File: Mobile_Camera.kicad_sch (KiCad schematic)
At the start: 22 parts, among them J1 SWD_header, J2 DVP_24_pin, J3 Micro_SD_card, SW1 Switch_reset, SW2 Switch_power_on, U1 STM32H753VIT6, Y1 Crystal

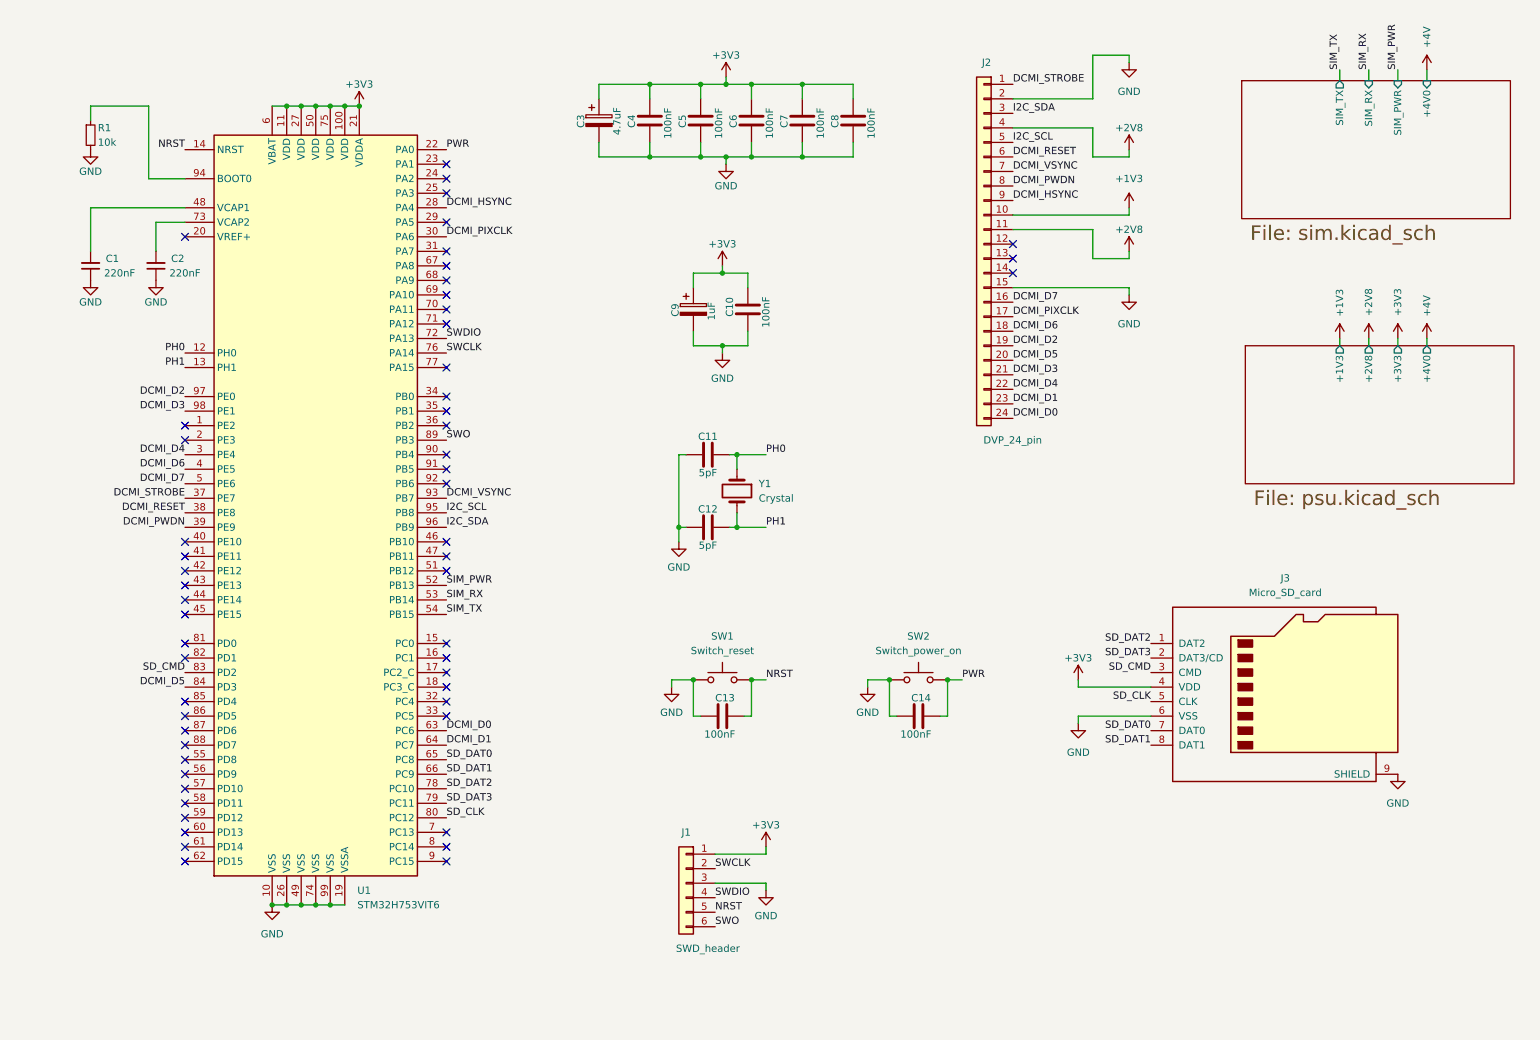
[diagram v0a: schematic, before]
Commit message: Complete the schematic, Begin to layout elements
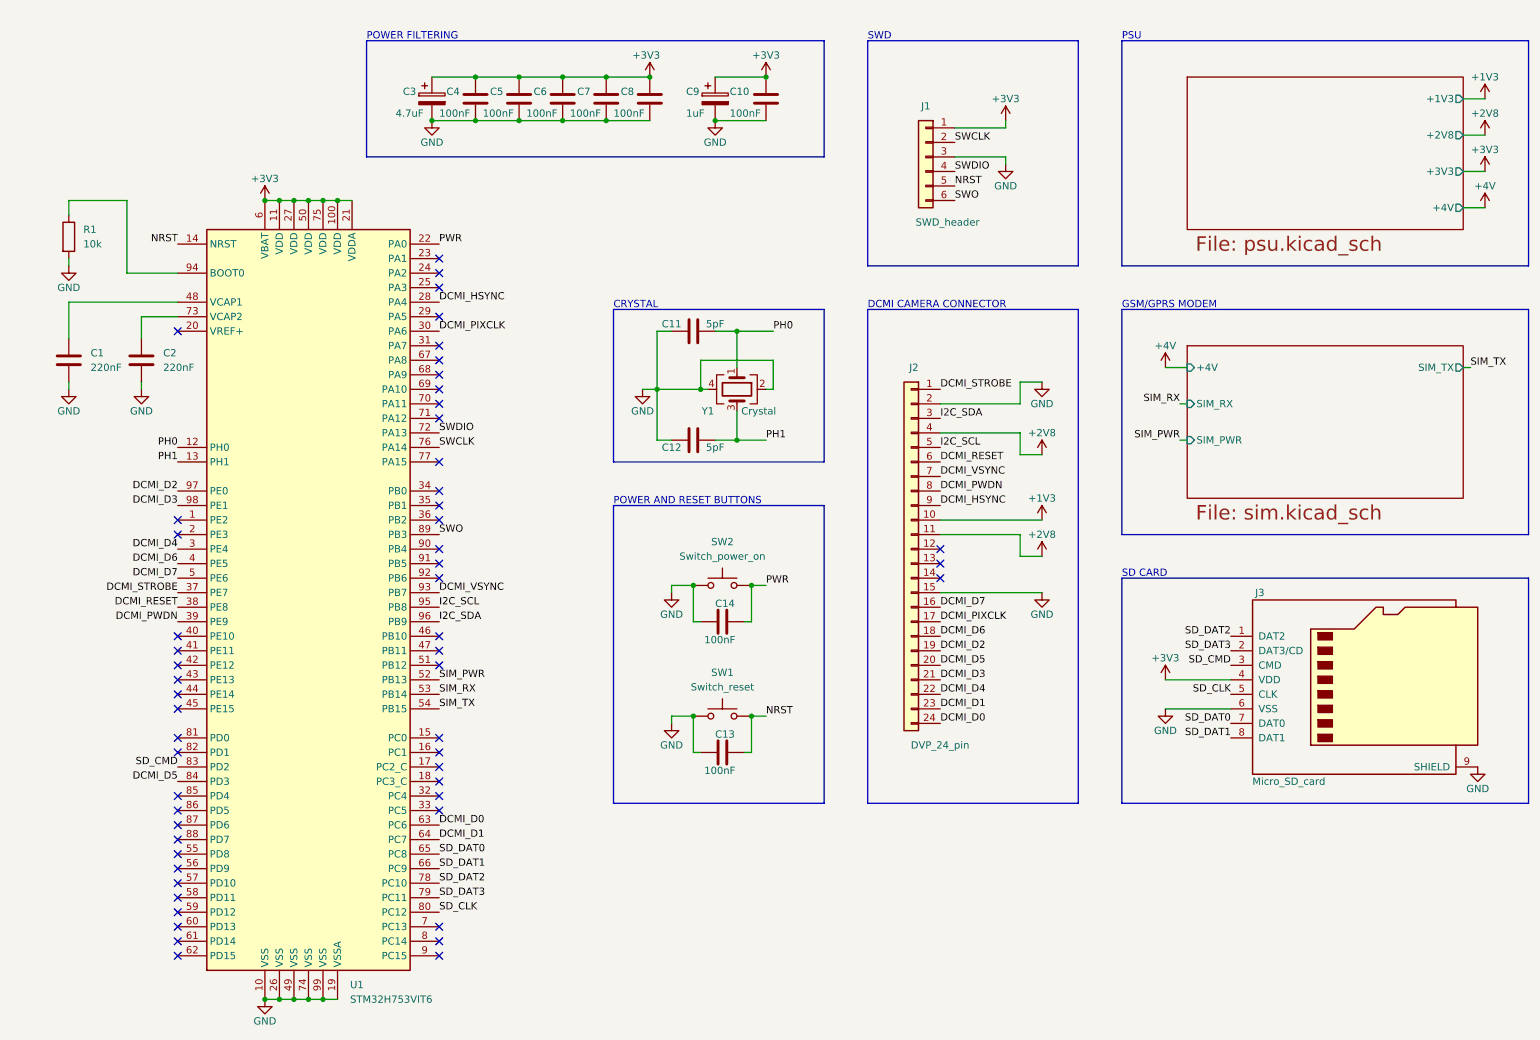
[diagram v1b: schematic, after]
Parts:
- removed C1, C2: 220nF, Capacitor_SMD:C_0603_1608Metric_Pad1.08x0.95mm_HandSolder, symbol Device:C_Small
- removed R1: 10k, Resistor_SMD:R_0603_1608Metric_Pad0.98x0.95mm_HandSolder, symbol Device:R_Small
- removed Y1: Crystal, Crystal:Crystal_SMD_SeikoEpson_TSX3225-4Pin_3.2x2.5mm_HandSoldering, symbol Device:Crystal
- added C1, C2: 220nF, Capacitor_SMD:C_0603_1608Metric_Pad1.08x0.95mm_HandSolder, symbol Device:C
- added R1: 10k, Resistor_SMD:R_0603_1608Metric_Pad0.98x0.95mm_HandSolder, symbol Device:R
- added Y1: Crystal, Crystal:Crystal_SMD_SeikoEpson_TSX3225-4Pin_3.2x2.5mm_HandSoldering, symbol Device:Crystal_GND24
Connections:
- net GND: now also C1.2, C2.2, R1.2, Y1.2, Y1.4
- net PH0: now also Y1.1
- net PH1: now also Y1.3
- net at U1.48 (VCAP1): now also C1.1
- net at U1.73 (VCAP2): now also C2.1
- net at U1.94 (BOOT0): now also R1.1
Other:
- sheet PSU ports: added +4V; removed +4V0
- sheet SIM ports: added +4V; removed +4V0
- note added: "CRYSTAL"
- note added: "DCMI CAMERA CONNECTOR"
- note added: "GSM/GPRS MODEM"
- note added: "POWER AND RESET BUTTONS"
- note added: "POWER FILTERING"
- note added: "PSU"
- note added: "SD CARD"
- note added: "SWD"
- moved on the sheet: C10, C11, C12, C13, C14, C3, C4, C5, C6, C7, C8, C9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

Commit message: Partial layout
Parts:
- removed SW1: Switch_reset, Button_Switch_SMD:SW_SPST_Omron_B3FS-101xP, symbol Switch:SW_MEC_5G
- removed SW2: Switch_power_on, Button_Switch_SMD:SW_SPST_Omron_B3FS-101xP, symbol Switch:SW_MEC_5G
- added SW1: SW_Power_On, Button_Switch_SMD:SW_SPST_Omron_B3FS-101xP, symbol Switch:SW_Omron_B3FS
- added SW2: SW_Reset, Button_Switch_SMD:SW_SPST_Omron_B3FS-101xP, symbol Switch:SW_Omron_B3FS
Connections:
- net GND: now also J2.MP, SW1.1, SW2.1
- net NRST: now also SW2.2
- net PWR: now also SW1.2
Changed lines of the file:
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@@
   (junction (at 102.87 36.83) (diameter 0) (color 0 0 0 0)
   )
+  (junction (at 127 83.82) (diameter 0) (color 0 0 0 0)
+  )
+  (junction (at 118.11 29.21) (diameter 0) (color 0 0 0 0)
+  )
   (junction (at 143.51 118.11) (diameter 0) (color 0 0 0 0)
   )
-  (junction (at 127 83.82) (diameter 0) (color 0 0 0 0)
-  )
-  (junction (at 118.11 29.21) (diameter 0) (color 0 0 0 0)
+  (junction (at 143.51 140.97) (diameter 0) (color 0 0 0 0)
   )
   (junction (at 95.25 29.21) (diameter 0) (color 0 0 0 0)
   )
-  (junction (at 143.51 140.97) (diameter 0) (color 0 0 0 0)
-  )
   (junction (at 60.96 190.5) (diameter 0) (color 0 0 0 0)
   )
@@
   (junction (at 95.25 36.83) (diameter 0) (color 0 0 0 0)
   )
+  (junction (at 133.35 140.97) (diameter 0) (color 0 0 0 0)
+  )
   (junction (at 63.5 50.8) (diameter 0) (color 0 0 0 0)
   )
@@
   )
   (junction (at 63.5 190.5) (diameter 0) (color 0 0 0 0)
-  )
-  (junction (at 133.35 140.97) (diameter 0) (color 0 0 0 0)
   )
   (junction (at 68.58 50.8) (diameter 0) (color 0 0 0 0)
@@
   )
   (wire (pts (xy 36.83 71.12) (xy 36.83 74.93))
+    (stroke (width 0) (type default))
+  )
+  (wire (pts (xy 176.53 144.78) (xy 194.31 144.78))
     (stroke (width 0) (type default))
   )
@@
     )
   )
+  (symbol (lib_id "Switch:SW_Omron_B3FS") (at 138.43 118.11 0) (unit 1)
+    (in_bom yes) (on_board yes) (dnp no) (fields_autoplaced)
+    (property "Reference" "SW1" (at 138.43 110.49 0)
+      (effects (font (size 1.27 1.27)))
+    )
+    (property "Value" "SW_Power_On" (at 138.43 113.03 0)
+      (effects (font (size 1.27 1.27)))
+    )
+    (property "Footprint" "Button_Switch_SMD:SW_SPST_Omron_B3FS-101xP" (at 138.43 113.03 0)
+      (effects (font (size 1.27 1.27)) hide)
+    )
+    (property "Datasheet" "https://omronfs.omron.com/en_US/ecb/products/pdf/en-b3fs.pdf" (at 138.43 113.03 0)
+      (effects (font (size 1.27 1.27)) hide)
+    )
+    (pin "1")
+    (pin "2")
+    (instances
+      (project "Mobile_Camera"
+        (path "/488cc6d2-d16d-430c-bbb5-58870e95eca1"
+          (reference "SW1") (unit 1)
+        )
+      )
+    )
+  )
   (symbol (lib_id "power:+3V3") (at 215.9 134.62 0) (unit 1)
     (in_bom yes) (on_board yes) (dnp no)
@@
     )
   )
-  (symbol (lib_id "Switch:SW_MEC_5G") (at 138.43 140.97 0) (unit 1)
+  (symbol (lib_id "Switch:SW_Omron_B3FS") (at 138.43 140.97 0) (unit 1)
     (in_bom yes) (on_board yes) (dnp no) (fields_autoplaced)
-    (property "Reference" "SW1" (at 138.43 133.35 0)
-      (effects (font (size 1.27 1.27)))
-    )
-    (property "Value" "Switch_reset" (at 138.43 135.89 0)
+    (property "Reference" "SW2" (at 138.43 133.35 0)
+      (effects (font (size 1.27 1.27)))
+    )
+    (property "Value" "SW_Reset" (at 138.43 135.89 0)
       (effects (font (size 1.27 1.27)))
     )
@@
       (effects (font (size 1.27 1.27)) hide)
     )
-    (property "Datasheet" "~" (at 138.43 135.89 0)
-      (effects (font (size 1.27 1.27)) hide)
-    )
-    (pin "1")
-    (pin "3")
+    (property "Datasheet" "https://omronfs.omron.com/en_US/ecb/products/pdf/en-b3fs.pdf" (at 138.43 135.89 0)
+      (effects (font (size 1.27 1.27)) hide)
+    )
+    (pin "1")
     (pin "2")
-    (pin "4")
-    (instances
-      (project "Mobile_Camera"
-        (path "/2b80fb81-335f-4975-adf0-2af3158761c0"
-          (reference "SW1") (unit 1)
-        )
-      )
-      (project "Mobile_Camera"
-        (path "/488cc6d2-d16d-430c-bbb5-58870e95eca1"
-          (reference "SW1") (unit 1)
-        )
-      )
-      (project "Mobile_Camera"
-        (path "/e63e39d7-6ac0-4ffd-8aa3-1841a4541b55"
-          (reference "SW1") (unit 1)
+    (instances
+      (project "Mobile_Camera"
+        (path "/488cc6d2-d16d-430c-bbb5-58870e95eca1"
+          (reference "SW2") (unit 1)
         )
       )
@@
     )
   )
+  (symbol (lib_id "power:GND") (at 194.31 144.78 0) (unit 1)
+    (in_bom yes) (on_board yes) (dnp no)
+    (property "Reference" "#PWR0103" (at 194.31 151.13 0)
+      (effects (font (size 1.27 1.27)) hide)
+    )
+    (property "Value" "GND" (at 194.31 148.59 0)
+      (effects (font (size 1.27 1.27)))
+    )
+    (property "Footprint" "" (at 194.31 144.78 0)
+      (effects (font (size 1.27 1.27)) hide)
+    )
+    (property "Datasheet" "" (at 194.31 144.78 0)
+      (effects (font (size 1.27 1.27)) hide)
+    )
+    (pin "1")
+    (instances
+      (project "Mobile_Camera"
+        (path "/2b80fb81-335f-4975-adf0-2af3158761c0"
+          (reference "#PWR0103") (unit 1)
+        )
+      )
+      (project "Mobile_Camera"
+        (path "/488cc6d2-d16d-430c-bbb5-58870e95eca1"
+          (reference "#PWR013") (unit 1)
+        )
+      )
+      (project "Mobile_Camera"
+        (path "/e63e39d7-6ac0-4ffd-8aa3-1841a4541b55"
+          (reference "#PWR0103") (unit 1)
+        )
+      )
+    )
+  )
   (symbol (lib_id "power:GND") (at 87.63 36.83 0) (unit 1)
     (in_bom yes) (on_board yes) (dnp no)
@@
         (path "/e63e39d7-6ac0-4ffd-8aa3-1841a4541b55"
           (reference "C6") (unit 1)
-        )
-      )
-    )
-  )
-  (symbol (lib_id "Switch:SW_MEC_5G") (at 138.43 118.11 0) (unit 1)
-    (in_bom yes) (on_board yes) (dnp no)
-    (property "Reference" "SW2" (at 138.43 110.49 0)
-      (effects (font (size 1.27 1.27)))
-    )
-    (property "Value" "Switch_power_on" (at 138.43 113.03 0)
-      (effects (font (size 1.27 1.27)))
-    )
-    (property "Footprint" "Button_Switch_SMD:SW_SPST_Omron_B3FS-101xP" (at 138.43 113.03 0)
-      (effects (font (size 1.27 1.27)) hide)
-    )
-    (property "Datasheet" "~" (at 138.43 113.03 0)
-      (effects (font (size 1.27 1.27)) hide)
-    )
-    (pin "1")
-    (pin "3")
-    (pin "2")
-    (pin "4")
-    (instances
-      (project "Mobile_Camera"
-        (path "/2b80fb81-335f-4975-adf0-2af3158761c0"
-          (reference "SW2") (unit 1)
-        )
-      )
-      (project "Mobile_Camera"
-        (path "/488cc6d2-d16d-430c-bbb5-58870e95eca1"
-          (reference "SW2") (unit 1)
-        )
-      )
-      (project "Mobile_Camera"
-        (path "/e63e39d7-6ac0-4ffd-8aa3-1841a4541b55"
-          (reference "SW2") (unit 1)
         )
       )
@@
       (effects (font (size 1.27 1.27)) (justify left))
     )
-    (property "Value" "DVP_24_pin" (at 181.61 146.05 0)
+    (property "Value" "DVP_24_pin" (at 180.34 148.59 0)
       (effects (font (size 1.27 1.27)) (justify left))
     )
@@
     (pin "8")
     (pin "9")
-    (instances
-      (project "Mobile_Camera"
+    (pin "MP")
+    (instances
+      (project "Mobile_Camera"

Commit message: Add layout and ednge cut
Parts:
- added H1, H2, H3, H4: MountingHole_Pad, MountingHole:MountingHole_3.2mm_M3_DIN965_Pad, symbol Mechanical:MountingHole_Pad
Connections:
- net GND: now also H1.1, H2.1, H3.1, H4.1
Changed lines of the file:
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@@
+    )
+  )
+  (symbol (lib_id "Mechanical:MountingHole_Pad") (at 46.99 34.29 0) (unit 1)
+    (in_bom yes) (on_board yes) (dnp no)
+    (property "Reference" "H2" (at 49.53 31.75 0)
+      (effects (font (size 1.27 1.27)) (justify left))
+    )
+    (property "Value" "MountingHole_Pad" (at 49.53 34.29 0)
+      (effects (font (size 1.27 1.27)) (justify left))
+    )
+    (property "Footprint" "MountingHole:MountingHole_3.2mm_M3_DIN965_Pad" (at 46.99 34.29 0)
+      (effects (font (size 1.27 1.27)) hide)
+    )
+    (property "Datasheet" "~" (at 46.99 34.29 0)
+      (effects (font (size 1.27 1.27)) hide)
+    )
+    (pin "1")
+    (instances
+      (project "Mobile_Camera"
+        (path "/488cc6d2-d16d-430c-bbb5-58870e95eca1"
+          (reference "H2") (unit 1)
+        )
+      )
+    )
+  )
+  (symbol (lib_name "GND_1") (lib_id "power:GND") (at 46.99 36.83 0) (unit 1)
+    (in_bom yes) (on_board yes) (dnp no) (fields_autoplaced)
+    (property "Reference" "#PWR017" (at 46.99 43.18 0)
+      (effects (font (size 1.27 1.27)) hide)
+    )
+    (property "Value" "GND" (at 46.99 41.91 0)
+      (effects (font (size 1.27 1.27)))
+    )
+    (property "Footprint" "" (at 46.99 36.83 0)
+      (effects (font (size 1.27 1.27)) hide)
+    )
+    (property "Datasheet" "" (at 46.99 36.83 0)
+      (effects (font (size 1.27 1.27)) hide)
+    )
+    (pin "1")
+    (instances
+      (project "Mobile_Camera"
+        (path "/488cc6d2-d16d-430c-bbb5-58870e95eca1"
+          (reference "#PWR017") (unit 1)
+        )
+      )
     )
   )
@@
         (path "/e63e39d7-6ac0-4ffd-8aa3-1841a4541b55"
           (reference "C10") (unit 1)
+        )
+      )
+    )
+  )
+  (symbol (lib_name "GND_1") (lib_id "power:GND") (at 22.86 36.83 0) (unit 1)
+    (in_bom yes) (on_board yes) (dnp no) (fields_autoplaced)
+    (property "Reference" "#PWR019" (at 22.86 43.18 0)
+      (effects (font (size 1.27 1.27)) hide)
+    )
+    (property "Value" "GND" (at 22.86 41.91 0)
+      (effects (font (size 1.27 1.27)))
+    )
+    (property "Footprint" "" (at 22.86 36.83 0)
+      (effects (font (size 1.27 1.27)) hide)
+    )
+    (property "Datasheet" "" (at 22.86 36.83 0)
+      (effects (font (size 1.27 1.27)) hide)
+    )
+    (pin "1")
+    (instances
+      (project "Mobile_Camera"
+        (path "/488cc6d2-d16d-430c-bbb5-58870e95eca1"
+          (reference "#PWR019") (unit 1)
         )
       )
@@
     )
   )
+  (symbol (lib_name "GND_1") (lib_id "power:GND") (at 46.99 24.13 0) (unit 1)
+    (in_bom yes) (on_board yes) (dnp no) (fields_autoplaced)
+    (property "Reference" "#PWR016" (at 46.99 30.48 0)
+      (effects (font (size 1.27 1.27)) hide)
+    )
+    (property "Value" "GND" (at 46.99 29.21 0)
+      (effects (font (size 1.27 1.27)))
+    )
+    (property "Footprint" "" (at 46.99 24.13 0)
+      (effects (font (size 1.27 1.27)) hide)
+    )
+    (property "Datasheet" "" (at 46.99 24.13 0)
+      (effects (font (size 1.27 1.27)) hide)
+    )
+    (pin "1")
+    (instances
+      (project "Mobile_Camera"
+        (path "/488cc6d2-d16d-430c-bbb5-58870e95eca1"
+          (reference "#PWR016") (unit 1)
+        )
+      )
+    )
+  )
   (symbol (lib_id "power:+3V3") (at 58.42 50.8 0) (unit 1)
     (in_bom yes) (on_board yes) (dnp no)
@@
     )
   )
+  (symbol (lib_name "GND_1") (lib_id "power:GND") (at 22.86 24.13 0) (unit 1)
+    (in_bom yes) (on_board yes) (dnp no) (fields_autoplaced)
+    (property "Reference" "#PWR018" (at 22.86 30.48 0)
+      (effects (font (size 1.27 1.27)) hide)
+    )
+    (property "Value" "GND" (at 22.86 29.21 0)
+      (effects (font (size 1.27 1.27)))
+    )
+    (property "Footprint" "" (at 22.86 24.13 0)
+      (effects (font (size 1.27 1.27)) hide)
+    )
+    (property "Datasheet" "" (at 22.86 24.13 0)
+      (effects (font (size 1.27 1.27)) hide)
+    )
+    (pin "1")
+    (instances
+      (project "Mobile_Camera"
+        (path "/488cc6d2-d16d-430c-bbb5-58870e95eca1"
+          (reference "#PWR018") (unit 1)
+        )
+      )
+    )
+  )
   (symbol (lib_id "power:+2V8") (at 271.78 39.37 0) (mirror y) (unit 1)
     (in_bom yes) (on_board yes) (dnp no)
@@
     )
   )
+  (symbol (lib_id "Mechanical:MountingHole_Pad") (at 22.86 21.59 0) (unit 1)
+    (in_bom yes) (on_board yes) (dnp no)
+    (property "Reference" "H3" (at 25.4 19.05 0)
+      (effects (font (size 1.27 1.27)) (justify left))
+    )
+    (property "Value" "MountingHole_Pad" (at 25.4 21.59 0)
+      (effects (font (size 1.27 1.27)) (justify left))
+    )
+    (property "Footprint" "MountingHole:MountingHole_3.2mm_M3_DIN965_Pad" (at 22.86 21.59 0)
+      (effects (font (size 1.27 1.27)) hide)
+    )
+    (property "Datasheet" "~" (at 22.86 21.59 0)
+      (effects (font (size 1.27 1.27)) hide)
+    )
+    (pin "1")
+    (instances
+      (project "Mobile_Camera"
+        (path "/488cc6d2-d16d-430c-bbb5-58870e95eca1"
+          (reference "H3") (unit 1)
+        )
+      )
+    )
+  )
   (symbol (lib_id "Device:C_Polarized") (at 87.63 33.02 0) (unit 1)
     (in_bom yes) (on_board yes) (dnp no)
@@
     )
   )
+  (symbol (lib_id "Mechanical:MountingHole_Pad") (at 46.99 21.59 0) (unit 1)
+    (in_bom yes) (on_board yes) (dnp no)
+    (property "Reference" "H1" (at 49.53 19.05 0)
+      (effects (font (size 1.27 1.27)) (justify left))
+    )
+    (property "Value" "MountingHole_Pad" (at 49.53 21.59 0)
+      (effects (font (size 1.27 1.27)) (justify left))
+    )
+    (property "Footprint" "MountingHole:MountingHole_3.2mm_M3_DIN965_Pad" (at 46.99 21.59 0)
+      (effects (font (size 1.27 1.27)) hide)
+    )
+    (property "Datasheet" "~" (at 46.99 21.59 0)
+      (effects (font (size 1.27 1.27)) hide)
+    )
+    (pin "1")
+    (instances
+      (project "Mobile_Camera"
+        (path "/488cc6d2-d16d-430c-bbb5-58870e95eca1"
+          (reference "H1") (unit 1)
+        )
+      )
+    )
+  )
   (symbol (lib_id "power:GND") (at 137.16 36.83 0) (unit 1)
     (in_bom yes) (on_board yes) (dnp no)
@@
         )
       )
+    )
+  )
+  (symbol (lib_id "Mechanical:MountingHole_Pad") (at 22.86 34.29 0) (unit 1)
+    (in_bom yes) (on_board yes) (dnp no)
+    (property "Reference" "H4" (at 25.4 31.75 0)
+      (effects (font (size 1.27 1.27)) (justify left))
+    )
+    (property "Value" "MountingHole_Pad" (at 25.4 34.29 0)
+      (effects (font (size 1.27 1.27)) (justify left))
+    )
+    (property "Footprint" "MountingHole:MountingHole_3.2mm_M3_DIN965_Pad" (at 22.86 34.29 0)
+      (effects (font (size 1.27 1.27)) hide)
+    )
+    (property "Datasheet" "~" (at 22.86 34.29 0)
+      (effects (font (size 1.27 1.27)) hide)
+    )
+    (pin "1")
+    (instances
+      (project "Mobile_Camera"
+        (path "/488cc6d2-d16d-430c-bbb5-58870e95eca1"
+          (reference "H4") (unit 1)
+        )
+      )
